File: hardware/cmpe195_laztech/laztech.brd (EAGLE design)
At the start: 68.6 x 61 mm, 27 parts

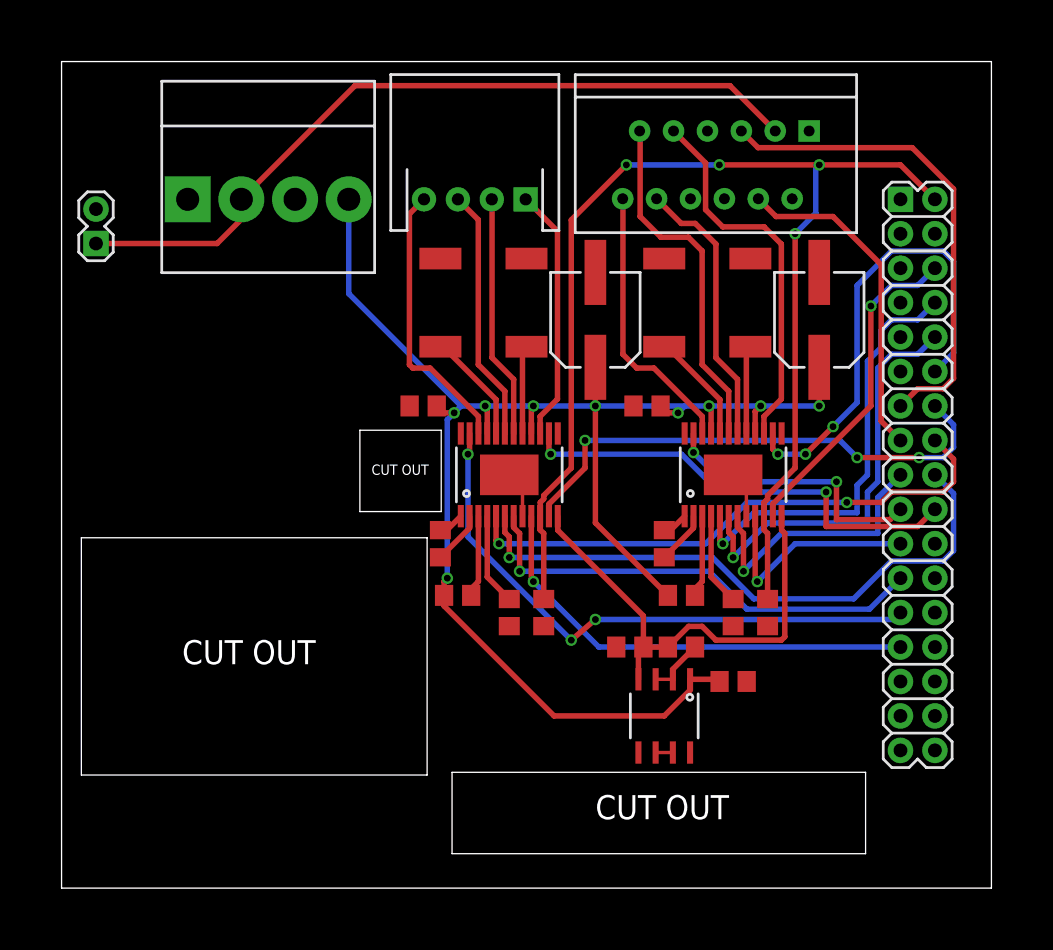
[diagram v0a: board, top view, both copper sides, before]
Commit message: Almost done with DRC fixes.
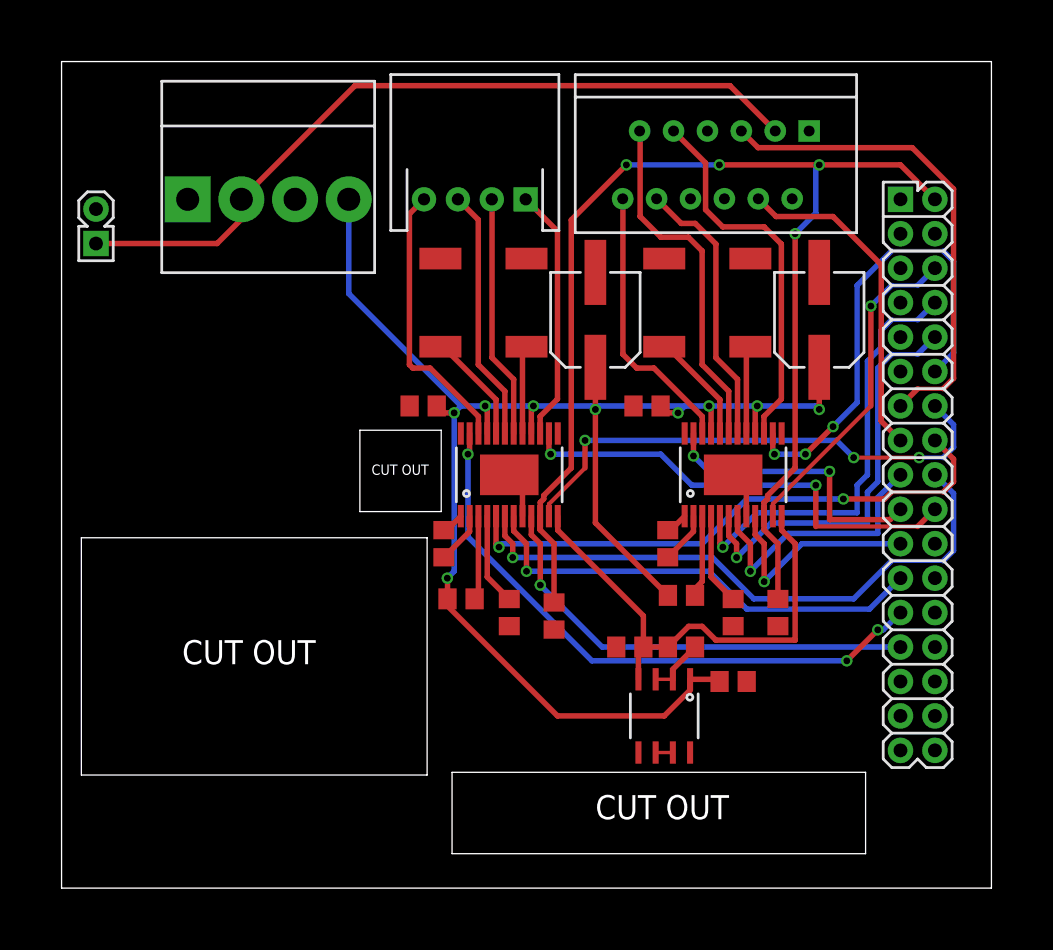
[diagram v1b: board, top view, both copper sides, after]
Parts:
- moved C2 0.80 mm to (36.3, 20.1)
- moved C1 0.76 mm to (52.8, 20.3)
- moved C8 0.36 mm to (29.5, 21.3)
- moved C5 0.25 mm to (44.7, 25.4)
- moved C6 0.25 mm to (28.2, 25.4)
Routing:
- net N$20: track 43.5 -> 44.8 mm
- net VREF: track 35.4 -> 36.6 mm
- net +3V3: track 93.4 -> 94.3 mm
- net N$24: track 20.7 -> 21.3 mm

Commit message: Finished board rev 1.
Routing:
- net N$34: track 5.60 -> 11.3 mm, vias 0 -> 2
- net GND: track 6.91 -> 11.3 mm, vias 0 -> 32
- net N$16: track 24.4 -> 27.9 mm
- net N$11: track 24.6 -> 27.3 mm
- net N$20: track 44.8 -> 46.9 mm
- net N$19: track 35.1 -> 37.1 mm
- net +5V: track 57.2 -> 56.1 mm
- net +3V3: track 94.3 -> 95.1 mm
- added copper zone on layer 1, net GND
- added copper zone on layer 16, net GND
